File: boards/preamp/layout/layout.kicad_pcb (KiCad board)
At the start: 4 copper layers, 0 parts

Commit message: 2.2 and slave headers moved
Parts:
- added C1: capacitor, C_0603_1608Metric, F.Cu at (32.0, 25.0)
- added C10: capacitor, C_0603_1608Metric, F.Cu at (50.0, 25.0)
- added C11: capacitor, C_0603_1608Metric, F.Cu at (68.0, 25.0)
- added C12: capacitor, C_0603_1608Metric, F.Cu at (86.0, 25.0)
- added C13: capacitor, C_0603_1608Metric, F.Cu at (104.0, 25.0)
- added C14: capacitor, C_0603_1608Metric, F.Cu at (122.0, 25.0)
- added C15: capacitor, C_0603_1608Metric, F.Cu at (140.0, 25.0)
- added C16: capacitor, C_0603_1608Metric, F.Cu at (158.0, 25.0)
- added C17: GRM21BZ71E106KE15K, C_0805_2012Metric, F.Cu at (32.0, 30.0)
- added C18: GRM21BZ71E106KE15K, C_0805_2012Metric, F.Cu at (50.0, 30.0)
- added C19: GRM21BZ71E106KE15K, C_0805_2012Metric, F.Cu at (68.0, 30.0)
- added C2: capacitor, C_0603_1608Metric, F.Cu at (86.0, 30.0)
- added C20: GRM21BZ71E106KE15K, C_0805_2012Metric, F.Cu at (104.0, 30.0)
- added C21: GRM21BZ71E106KE15K, C_0805_2012Metric, F.Cu at (122.0, 30.0)
- added C22: GRM21BZ71E106KE15K, C_0805_2012Metric, F.Cu at (140.0, 30.0)
- added C23: GRM21BZ71E106KE15K, C_0805_2012Metric, F.Cu at (158.0, 30.0)
- added C24: GRM21BZ71E106KE15K, C_0805_2012Metric, F.Cu at (32.0, 35.0)
- added C25: GCM1885C2A103JE02D, C_0603_1608Metric, F.Cu at (50.0, 35.0)
- added C26: GCM1885C2A103JE02D, C_0603_1608Metric, F.Cu at (68.0, 35.0)
- added C27: GCM1885C2A103JE02D, C_0603_1608Metric, F.Cu at (86.0, 35.0)
- added C28: GCM1885C2A103JE02D, C_0603_1608Metric, F.Cu at (104.0, 35.0)
- added C29: GCM1885C2A103JE02D, C_0603_1608Metric, F.Cu at (122.0, 35.0)
- added C3: capacitor, C_0603_1608Metric, F.Cu at (140.0, 35.0)
- added C30: GCM1885C2A103JE02D, C_0603_1608Metric, F.Cu at (158.0, 35.0)
- added C31: GCM1885C2A103JE02D, C_0603_1608Metric, F.Cu at (32.0, 40.0)
- added C32: GCM1885C2A103JE02D, C_0603_1608Metric, F.Cu at (50.0, 40.0)
- added C33: GRM21BZ71E106KE15K, C_0805_2012Metric, F.Cu at (68.0, 40.0)
- added C34: GRM21BZ71E106KE15K, C_0805_2012Metric, F.Cu at (86.0, 40.0)
- added C35: GRM21BZ71E106KE15K, C_0805_2012Metric, F.Cu at (104.0, 40.0)
- added C36: GRM21BZ71E106KE15K, C_0805_2012Metric, F.Cu at (122.0, 40.0)
- added C37: GRM21BZ71E106KE15K, C_0805_2012Metric, F.Cu at (140.0, 40.0)
- added C38: GRM21BZ71E106KE15K, C_0805_2012Metric, F.Cu at (158.0, 40.0)
- added C39: GRM21BZ71E106KE15K, C_0805_2012Metric, F.Cu at (32.0, 45.0)
- added C4: capacitor, C_0603_1608Metric, F.Cu at (50.0, 45.0)
- added C40: GRM21BZ71E106KE15K, C_0805_2012Metric, F.Cu at (68.0, 45.0)
- added C41: capacitor, C_1206_3216Metric, F.Cu at (86.0, 45.0)
- added C42: GRM188R72A104KA35D, C_0603_1608Metric, F.Cu at (104.0, 45.0)
- added C43: GRM21BZ71E106KE15K, C_0805_2012Metric, F.Cu at (122.0, 45.0)
- added C44: GRM188R72A104KA35D, C_0603_1608Metric, F.Cu at (140.0, 45.0)
- added C45: GRM21BZ71E106KE15K, C_0805_2012Metric, F.Cu at (158.0, 45.0)
- added C46: GRM188R72A104KA35D, C_0603_1608Metric, F.Cu at (32.0, 50.0)
- added C47: GRM21BZ71E106KE15K, C_0805_2012Metric, F.Cu at (50.0, 50.0)
- added C48: GRM188R72A104KA35D, C_0603_1608Metric, F.Cu at (68.0, 50.0)
- added C49: GRM21BZ71E106KE15K, C_0805_2012Metric, F.Cu at (86.0, 50.0)
- added C5: capacitor, C_0603_1608Metric, F.Cu at (104.0, 50.0)
- added C50: GRM188R72A104KA35D, C_0603_1608Metric, F.Cu at (122.0, 50.0)
- added C51: GRM21BZ71E106KE15K, C_0805_2012Metric, F.Cu at (140.0, 50.0)
- added C52: GRM188R72A104KA35D, C_0603_1608Metric, F.Cu at (158.0, 50.0)
- added C53: GRM21BZ71E106KE15K, C_0805_2012Metric, F.Cu at (32.0, 55.0)
- added C54: GRM188R72A104KA35D, C_0603_1608Metric, F.Cu at (50.0, 55.0)
- added C55: GRM21BZ71E106KE15K, C_0805_2012Metric, F.Cu at (68.0, 55.0)
- added C56: GRM188R72A104KA35D, C_0603_1608Metric, F.Cu at (86.0, 55.0)
- added C57: GRM21BZ71E106KE15K, C_0805_2012Metric, F.Cu at (104.0, 55.0)
- added C58: GRM188R72A104KA35D, C_0603_1608Metric, F.Cu at (122.0, 55.0)
- added C59: GRM21BZ71E106KE15K, C_0805_2012Metric, F.Cu at (140.0, 55.0)
- added C6: capacitor, C_0603_1608Metric, F.Cu at (158.0, 55.0)
- added C60: GRM188R72A104KA35D, C_0603_1608Metric, F.Cu at (32.0, 60.0)
- added C61: GRM21BZ71E106KE15K, C_0805_2012Metric, F.Cu at (50.0, 60.0)
- added C62: GRM188R72A104KA35D, C_0603_1608Metric, F.Cu at (68.0, 60.0)
- added C63: GRM21BZ71E106KE15K, C_0805_2012Metric, F.Cu at (86.0, 60.0)
- added C64: GRM188R72A104KA35D, C_0603_1608Metric, F.Cu at (104.0, 60.0)
- added C65: GRM21BZ71E106KE15K, C_0805_2012Metric, F.Cu at (122.0, 60.0)
- added C66: GRM188R72A104KA35D, C_0603_1608Metric, F.Cu at (140.0, 60.0)
- added C67: GRM21BZ71E106KE15K, C_0805_2012Metric, F.Cu at (158.0, 60.0)
- added C68: GRM188R72A104KA35D, C_0603_1608Metric, F.Cu at (32.0, 65.0)
- added C69: GRM21BZ71E106KE15K, C_0805_2012Metric, F.Cu at (50.0, 65.0)
- added C7: capacitor, C_0603_1608Metric, F.Cu at (68.0, 65.0)
- added C70: GRM188R72A104KA35D, C_0603_1608Metric, F.Cu at (86.0, 65.0)
- added C71: GRM21BZ71E106KE15K, C_0805_2012Metric, F.Cu at (104.0, 65.0)
- added C72: GRM188R72A104KA35D, C_0603_1608Metric, F.Cu at (122.0, 65.0)
- added C73: GRM21BZ71E106KE15K, C_0805_2012Metric, F.Cu at (140.0, 65.0)
- added C74: GRM188R72A104KA35D, C_0603_1608Metric, F.Cu at (158.0, 65.0)
- added C75: GRM21BZ71E106KE15K, C_0805_2012Metric, F.Cu at (32.0, 70.0)
- added C76: GRM188R72A104KA35D, C_0603_1608Metric, F.Cu at (50.0, 70.0)
- added C8: capacitor, C_0603_1608Metric, F.Cu at (68.0, 70.0)
- added C9: capacitor, C_0603_1608Metric, F.Cu at (86.0, 70.0)
- added H1: ?, MountingHole_3.2mm_M3_DIN965_Pad_TopBottom, F.Cu at (13.0, 13.0)
- added H2: ?, MountingHole_3.2mm_M3_DIN965_Pad_TopBottom, F.Cu at (167.0, 13.0)
- added H3: ?, MountingHole_3.2mm_M3_DIN965_Pad_TopBottom, F.Cu at (13.0, 87.0)
- added H4: ?, MountingHole_3.2mm_M3_DIN965_Pad_TopBottom, F.Cu at (167.0, 87.0)
- added J1: NMJ6HF2, Jack_6.35mm_Neutrik_NMJ6HFD2_Horizontal, F.Cu at (25.0, 75.0)
- added J10: 61300211121, PinHeader_1x02_P2.54mm_Vertical, F.Cu at (133.0, 75.0)
- added J11: 61300211121, PinHeader_1x02_P2.54mm_Vertical, F.Cu at (145.0, 75.0)
- added J12: 61300211121, PinHeader_1x02_P2.54mm_Vertical, F.Cu at (157.0, 75.0)
- added J13: 61300211121, PinHeader_1x02_P2.54mm_Vertical, F.Cu at (25.0, 80.0)
- added J14: 61300211121, PinHeader_1x02_P2.54mm_Vertical, F.Cu at (37.0, 80.0)
- added J15: 61300211121, PinHeader_1x02_P2.54mm_Vertical, F.Cu at (49.0, 80.0)
- added J16: 61300211121, PinHeader_1x02_P2.54mm_Vertical, F.Cu at (61.0, 80.0)
- added J17: 61301021121, PinHeader_2x05_P2.54mm_Vertical, F.Cu at (73.0, 80.0)
- added J18: 61300211121, PinHeader_1x02_P2.54mm_Vertical, F.Cu at (85.0, 80.0)
- added J2: NMJ6HF2, Jack_6.35mm_Neutrik_NMJ6HFD2_Horizontal, F.Cu at (37.0, 75.0)
- added J3: NMJ6HF2, Jack_6.35mm_Neutrik_NMJ6HFD2_Horizontal, F.Cu at (49.0, 75.0)
- added J4: NMJ6HF2, Jack_6.35mm_Neutrik_NMJ6HFD2_Horizontal, F.Cu at (61.0, 75.0)
- added J5: NMJ6HF2, Jack_6.35mm_Neutrik_NMJ6HFD2_Horizontal, F.Cu at (73.0, 75.0)
- added J6: NMJ6HF2, Jack_6.35mm_Neutrik_NMJ6HFD2_Horizontal, F.Cu at (85.0, 75.0)
- added J7: NMJ6HF2, Jack_6.35mm_Neutrik_NMJ6HFD2_Horizontal, F.Cu at (97.0, 75.0)
- added J8: NMJ6HF2, Jack_6.35mm_Neutrik_NMJ6HFD2_Horizontal, F.Cu at (109.0, 75.0)
- added J9: 61300211121, PinHeader_1x02_P2.54mm_Vertical, F.Cu at (121.0, 75.0)
- added R1: ERJ-3EKF7501V, R_0603_1608Metric, F.Cu at (34.0, 25.0)
- added R10: ERJ-3EKF7501V, R_0603_1608Metric, F.Cu at (52.0, 25.0)
- added R11: ERJ-3EKF7501V, R_0603_1608Metric, F.Cu at (70.0, 25.0)
- added R12: ERJ-3EKF7501V, R_0603_1608Metric, F.Cu at (88.0, 25.0)
- added R13: ERJ-3EKF7501V, R_0603_1608Metric, F.Cu at (106.0, 25.0)
- added R14: ERJ-3EKF7501V, R_0603_1608Metric, F.Cu at (124.0, 25.0)
- added R15: ERJ-3EKF7501V, R_0603_1608Metric, F.Cu at (142.0, 25.0)
- added R16: ERJ-3EKF7501V, R_0603_1608Metric, F.Cu at (160.0, 25.0)
- added R17: ERJ-3EKF1004V, R_0603_1608Metric, F.Cu at (34.0, 30.0)
- added R18: ERJ-3EKF1004V, R_0603_1608Metric, F.Cu at (52.0, 30.0)
- added R19: ERJ-3EKF1004V, R_0603_1608Metric, F.Cu at (70.0, 30.0)
- added R2: ERJ-3EKF7501V, R_0603_1608Metric, F.Cu at (88.0, 30.0)
- added R20: ERJ-3EKF1004V, R_0603_1608Metric, F.Cu at (106.0, 30.0)
- added R21: ERJ-3EKF1004V, R_0603_1608Metric, F.Cu at (124.0, 30.0)
- added R22: ERJ-3EKF1004V, R_0603_1608Metric, F.Cu at (142.0, 30.0)
- added R23: ERJ-3EKF1004V, R_0603_1608Metric, F.Cu at (160.0, 30.0)
- added R24: ERJ-3EKF1004V, R_0603_1608Metric, F.Cu at (34.0, 35.0)
- added R25: ERJ-3EKF1002V, R_0603_1608Metric, F.Cu at (52.0, 35.0)
- added R26: ERJ-3EKF1002V, R_0603_1608Metric, F.Cu at (70.0, 35.0)
- added R27: resistor, R_0603_1608Metric, F.Cu at (88.0, 35.0)
- added R28: resistor, R_0603_1608Metric, F.Cu at (106.0, 35.0)
- added R29: resistor, R_0603_1608Metric, F.Cu at (124.0, 35.0)
- added R3: ERJ-3EKF7501V, R_0603_1608Metric, F.Cu at (142.0, 35.0)
- added R30: resistor, R_0603_1608Metric, F.Cu at (160.0, 35.0)
- added R31: resistor, R_0603_1608Metric, F.Cu at (34.0, 40.0)
- added R32: resistor, R_0603_1608Metric, F.Cu at (52.0, 40.0)
- added R33: resistor, R_0603_1608Metric, F.Cu at (70.0, 40.0)
- added R34: resistor, R_0603_1608Metric, F.Cu at (88.0, 40.0)
- added R35: ERJ-3EKF1001V, R_0603_1608Metric, F.Cu at (106.0, 40.0)
- added R36: ERJ-3EKF1001V, R_0603_1608Metric, F.Cu at (124.0, 40.0)
- added R37: ERJ-3EKF1001V, R_0603_1608Metric, F.Cu at (142.0, 40.0)
- added R38: ERJ-3EKF1001V, R_0603_1608Metric, F.Cu at (160.0, 40.0)
- added R39: ERJ-3EKF1001V, R_0603_1608Metric, F.Cu at (34.0, 45.0)
- added R4: ERJ-3EKF7501V, R_0603_1608Metric, F.Cu at (52.0, 45.0)
- added R40: ERJ-3EKF1001V, R_0603_1608Metric, F.Cu at (70.0, 45.0)
- added R41: ERJ-3EKF1001V, R_0603_1608Metric, F.Cu at (88.0, 45.0)
- added R42: ERJ-3EKF1001V, R_0603_1608Metric, F.Cu at (106.0, 45.0)
- added R5: ERJ-3EKF7501V, R_0603_1608Metric, F.Cu at (124.0, 45.0)
- added R6: ERJ-3EKF7501V, R_0603_1608Metric, F.Cu at (142.0, 45.0)
- added R7: ERJ-3EKF7501V, R_0603_1608Metric, F.Cu at (160.0, 45.0)
- added R8: ERJ-3EKF7501V, R_0603_1608Metric, F.Cu at (34.0, 50.0)
- added R9: ERJ-3EKF7501V, R_0603_1608Metric, F.Cu at (52.0, 50.0)
- added RV1: 3296W-1-103LF, Potentiometer_Bourns_3296W_Vertical, F.Cu at (70.0, 50.0)
- added RV2: 3296W-1-103LF, Potentiometer_Bourns_3296W_Vertical, F.Cu at (88.0, 50.0)
- added RV3: 3296W-1-103LF, Potentiometer_Bourns_3296W_Vertical, F.Cu at (106.0, 50.0)
- added RV4: 3296W-1-103LF, Potentiometer_Bourns_3296W_Vertical, F.Cu at (124.0, 50.0)
- added RV5: 3296W-1-103LF, Potentiometer_Bourns_3296W_Vertical, F.Cu at (142.0, 50.0)
- added RV6: 3296W-1-103LF, Potentiometer_Bourns_3296W_Vertical, F.Cu at (160.0, 50.0)
- added RV7: 3296W-1-103LF, Potentiometer_Bourns_3296W_Vertical, F.Cu at (34.0, 55.0)
- added RV8: 3296W-1-103LF, Potentiometer_Bourns_3296W_Vertical, F.Cu at (52.0, 55.0)
- added U1: NE5532DR, SOIC-8_3.9x4.9mm_P1.27mm, F.Cu at (30.0, 30.0)
- added U10: NE5532DR, SOIC-8_3.9x4.9mm_P1.27mm, F.Cu at (48.0, 30.0)
- added U11: NE5532DR, SOIC-8_3.9x4.9mm_P1.27mm, F.Cu at (66.0, 30.0)
- added U12: NE5532DR, SOIC-8_3.9x4.9mm_P1.27mm, F.Cu at (84.0, 30.0)
- added U13: NE5532DR, SOIC-8_3.9x4.9mm_P1.27mm, F.Cu at (102.0, 30.0)
- added U14: NE5532DR, SOIC-8_3.9x4.9mm_P1.27mm, F.Cu at (120.0, 30.0)
- added U15: NE5532DR, SOIC-8_3.9x4.9mm_P1.27mm, F.Cu at (138.0, 30.0)
- added U16: NE5532DR, SOIC-8_3.9x4.9mm_P1.27mm, F.Cu at (156.0, 30.0)
- added U17: NE5532DR, SOIC-8_3.9x4.9mm_P1.27mm, F.Cu at (30.0, 45.0)
- added U2: NE5532DR, SOIC-8_3.9x4.9mm_P1.27mm, F.Cu at (48.0, 45.0)
- added U3: NE5532DR, SOIC-8_3.9x4.9mm_P1.27mm, F.Cu at (66.0, 45.0)
- added U4: NE5532DR, SOIC-8_3.9x4.9mm_P1.27mm, F.Cu at (84.0, 45.0)
- added U5: NE5532DR, SOIC-8_3.9x4.9mm_P1.27mm, F.Cu at (102.0, 45.0)
- added U6: NE5532DR, SOIC-8_3.9x4.9mm_P1.27mm, F.Cu at (120.0, 45.0)
- added U7: NE5532DR, SOIC-8_3.9x4.9mm_P1.27mm, F.Cu at (138.0, 45.0)
- added U8: NE5532DR, SOIC-8_3.9x4.9mm_P1.27mm, F.Cu at (156.0, 45.0)
- added U9: NE5532DR, SOIC-8_3.9x4.9mm_P1.27mm, F.Cu at (30.0, 60.0)
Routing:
- added copper zone on B.Cu, net GND
- added copper zone on F.Cu, net GND
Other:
- board outline added: 160 x 80 mm

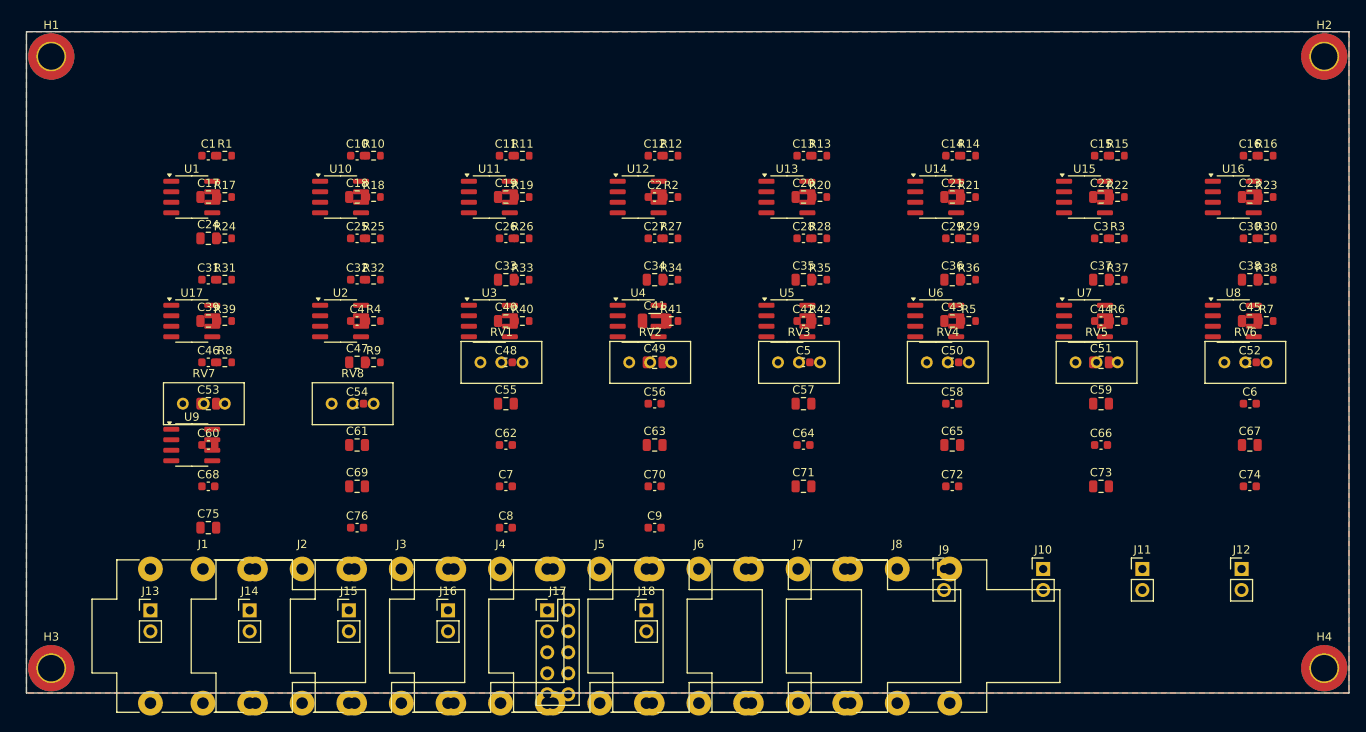
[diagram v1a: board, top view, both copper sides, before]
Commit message: layout changes, main boards smaller
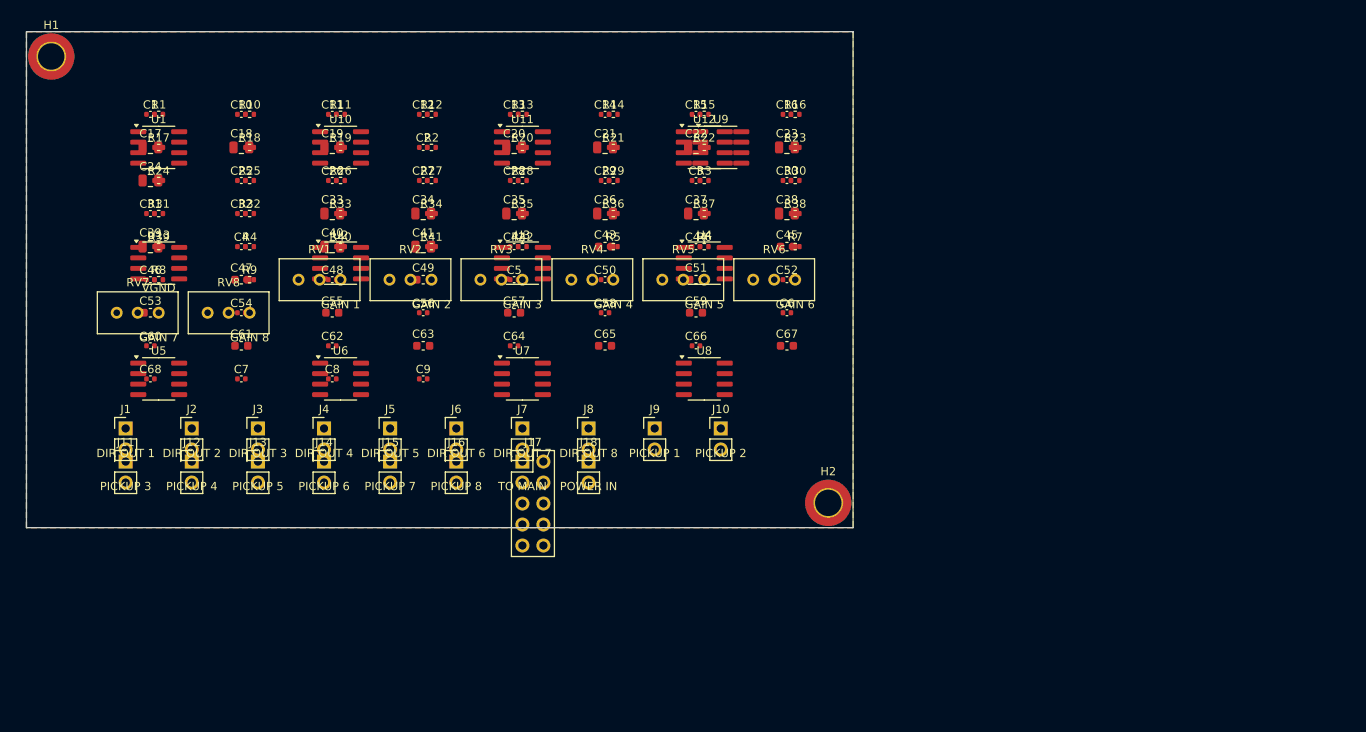
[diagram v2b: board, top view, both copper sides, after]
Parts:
- removed C69, C71, C73, C75: GRM21BZ71E106KE15K, C_0805_2012Metric
- removed C70, C72, C74, C76: GRM188R72A104KA35D, C_0603_1608Metric
- removed H3, H4: ?, MountingHole_3.2mm_M3_DIN965_Pad_TopBottom
- removed U14, U15, U16, U17: NE5532DR, SOIC-8_3.9x4.9mm_P1.27mm
- C1, C10, C11, C12, C13, C14, C15, C16, C2, C3, C4, C5, C6, C7, C8, C9: value capacitor -> GCM1555C1H102FA16D; footprint C_0603_1608Metric -> C_0402_1005Metric
- C25, C26, C27, C28, C29, C30, C31, C32: value GCM1885C2A103JE02D -> GRM1555CYA103GE01D; footprint C_0603_1608Metric -> C_0402_1005Metric
- C41: footprint C_1206_3216Metric -> C_0805_2012Metric
- C42, C44, C46, C48, C50, C52, C54, C56, C58, C60, C62, C64, C66, C68: value GRM188R72A104KA35D -> GCM155R71H104KE02D; footprint C_0603_1608Metric -> C_0402_1005Metric
- C43, C45, C47, C49, C51, C53, C55, C57, C59, C61, C63, C65, C67: value GRM21BZ71E106KE15K -> GRM188Z71A106KA73D; footprint C_0805_2012Metric -> C_0603_1608Metric
- J1, J2, J3, J4, J5, J6, J7, J8: value NMJ6HF2 -> 61300211121; footprint Jack_6.35mm_Neutrik_NMJ6HFD2_Horizontal -> PinHeader_1x02_P2.54mm_Vertical
- R1, R10, R11, R12, R13, R14, R15, R16, R2, R3, R4, R5, R6, R7, R8, R9: value ERJ-3EKF7501V -> ERJ-2RKF7501X; footprint R_0603_1608Metric -> R_0402_1005Metric
- R17, R18, R19, R20, R21, R22, R23, R24: value ERJ-3EKF1004V -> ERJ-2RKF1004X; footprint R_0603_1608Metric -> R_0402_1005Metric
- R25, R26: value ERJ-3EKF1002V -> ERJ-2RKF1002X; footprint R_0603_1608Metric -> R_0402_1005Metric
- R27, R28, R29, R30, R31, R32, R33, R34: footprint R_0603_1608Metric -> R_0402_1005Metric
- R35, R36, R37, R38, R39, R40, R41, R42: value ERJ-3EKF1001V -> ERJ-2RKF1001X; footprint R_0603_1608Metric -> R_0402_1005Metric
- moved J12 127.7 mm to (30.0, 62.0)
- moved J11 123.7 mm to (22.0, 62.0)
- moved H2 80.7 mm to (107.0, 67.0)
- moved U13 76.4 mm to (26.0, 38.0)
- moved U5 76.3 mm to (26.0, 52.0)
- moved U9 73.4 mm to (94.0, 24.0)
- moved U6 72.3 mm to (48.0, 52.0)
- moved U7 68.4 mm to (70.0, 52.0)
- moved U8 64.4 mm to (92.0, 52.0)
- moved RV6 57.9 mm to (103.0, 40.0)
- moved R7 57.7 mm to (103.0, 36.0)
- moved R38 57.6 mm to (103.0, 32.0)
- moved R30 57.4 mm to (103.0, 28.0)
- moved R23 57.3 mm to (103.0, 24.0)
- moved C67 57.3 mm to (102.0, 48.0)
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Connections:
- C17 pad 1: DIRECT_OUT_1 -> BUFFERED_1
- C18 pad 1: DIRECT_OUT_2 -> BUFFERED_2
- C19 pad 1: DIRECT_OUT_3 -> BUFFERED_3
- C20 pad 1: DIRECT_OUT_4 -> BUFFERED_4
- C21 pad 1: DIRECT_OUT_5 -> BUFFERED_5
- C22 pad 1: DIRECT_OUT_6 -> BUFFERED_6
- C23 pad 1: DIRECT_OUT_7 -> BUFFERED_7
- C24 pad 1: DIRECT_OUT_8 -> BUFFERED_8
- U10 pad 1: DIRECT_OUT_3 -> AMPLIFIED_3
- U10 pad 2: DIRECT_OUT_3 -> FB_3
- U10 pad 6: DIRECT_OUT_4 -> FB_4
- U10 pad 7: DIRECT_OUT_4 -> AMPLIFIED_4
- U11 pad 1: DIRECT_OUT_5 -> AMPLIFIED_5
- U11 pad 2: DIRECT_OUT_5 -> FB_5
- U11 pad 6: DIRECT_OUT_6 -> FB_6
- U11 pad 7: DIRECT_OUT_6 -> AMPLIFIED_6
- U12 pad 1: DIRECT_OUT_7 -> AMPLIFIED_7
- U12 pad 2: DIRECT_OUT_7 -> FB_7
- U12 pad 6: DIRECT_OUT_8 -> FB_8
- U12 pad 7: DIRECT_OUT_8 -> AMPLIFIED_8
- U13 pad 1: AMPLIFIED_1 -> VGND
- U13 pad 2: FB_1 -> VGND
- U13 pad 3: BUFFERED_1 -> VGND_MID
- U13 pad 5: BUFFERED_2 -> _IN_P
- U13 pad 6: FB_2 -> _IN_N
- U13 pad 7: AMPLIFIED_2 -> _OUT
- U9 pad 1: DIRECT_OUT_1 -> AMPLIFIED_1
- U9 pad 2: DIRECT_OUT_1 -> FB_1
- U9 pad 6: DIRECT_OUT_2 -> FB_2
- U9 pad 7: DIRECT_OUT_2 -> AMPLIFIED_2
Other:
- board size 160 x 80 mm -> 100 x 60 mm
- board text added: "DIR OUT 1"
- board text added: "DIR OUT 2"
- board text added: "DIR OUT 3"
- board text added: "DIR OUT 4"
- board text added: "DIR OUT 5"
- board text added: "DIR OUT 6"
- board text added: "DIR OUT 7"
- board text added: "DIR OUT 8"
- board text added: "GAIN 1"
- board text added: "GAIN 2"
- board text added: "GAIN 3"
- board text added: "GAIN 4"
- board text added: "GAIN 5"
- board text added: "GAIN 6"
- board text added: "GAIN 7"
- board text added: "GAIN 8"
- board text added: "PICKUP 1"
- board text added: "PICKUP 2"
- board text added: "PICKUP 3"
- board text added: "PICKUP 4"
- board text added: "PICKUP 5"
- board text added: "PICKUP 6"
- board text added: "PICKUP 7"
- board text added: "PICKUP 8"
- board text added: "POWER IN"
- board text added: "TO MAIN"
- board text added: "VGND"

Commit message: layout tweaks
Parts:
- moved R30 86.4 mm to (17.0, 36.0)
- moved J10 85.7 mm to (13.0, 86.0)
- moved RV7 82.2 mm to (104.0, 70.0)
- moved C29 77.1 mm to (27.0, 84.0)
- moved RV8 75.6 mm to (104.0, 79.0)
- moved R39 74.7 mm to (99.0, 52.0)
- moved C39 74.0 mm to (83.0, 82.0)
- moved R1 73.1 mm to (99.0, 16.0)
- moved C27 69.4 mm to (17.0, 84.0)
- moved C67 67.0 mm to (35.0, 46.0)
- moved C26 65.5 mm to (13.0, 84.0)
- moved R29 64.1 mm to (17.0, 32.0)
- moved J8 64.1 mm to (14.0, 54.5)
- moved C31 62.6 mm to (85.0, 14.0)
- moved RV1 60.9 mm to (104.0, 16.0)
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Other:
- board size 100 x 60 mm -> 100 x 80 mm

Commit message: layout fixes
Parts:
- RV1, RV2, RV3, RV4, RV5, RV6, RV7, RV8: value 3296W-1-103LF -> 3314J-1-103E; footprint Potentiometer_Bourns_3296W_Vertical -> Potentiometer_Bourns_3314J_Vertical
- moved C31 86.0 mm to (35.0, 84.0)
- moved C32 74.0 mm to (39.0, 84.0)
- moved C30 72.5 mm to (31.0, 84.0)
- moved C26 71.6 mm to (45.0, 20.0)
- moved R36 60.2 mm to (41.0, 40.0)
- moved C33 56.9 mm to (75.0, 88.0)
- moved C34 47.7 mm to (79.0, 82.0)
- moved C3 46.5 mm to (103.0, 30.0)
- moved R42 39.8 mm to (99.0, 78.0)
- moved R41 39.4 mm to (103.0, 74.0)
- moved R38 38.5 mm to (61.0, 36.0)
- moved C5 38.0 mm to (103.0, 48.0)
- moved C36 36.7 mm to (61.0, 50.0)
- moved C7 20.0 mm to (103.0, 66.0)
- moved C2 14.0 mm to (35.0, 34.0)
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
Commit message: layout
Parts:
- moved C1 77.9 mm to (103.0, 12.0)
- moved C31 77.7 mm to (79.0, 20.0)
- moved C27 69.3 mm to (55.0, 26.0)
- moved C25 64.8 mm to (45.0, 84.0)
- moved R36 59.7 mm to (99.0, 26.0)
- moved R2 58.3 mm to (99.0, 24.0)
- moved C46 57.7 mm to (91.0, 50.0)
- moved C33 56.9 mm to (39.0, 44.0)
- moved C65 56.0 mm to (35.0, 22.0)
- moved R4 50.0 mm to (99.0, 44.0)
- moved C34 47.7 mm to (39.0, 56.0)
- moved R41 46.6 mm to (79.0, 34.0)
- moved C3 46.5 mm to (61.0, 50.0)
- moved C59 45.7 mm to (85.0, 26.0)
- moved R40 42.8 mm to (99.0, 60.0)
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
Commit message: yout
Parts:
- added C69: GCM155R71H104KE02D, C_0402_1005Metric, F.Cu at (57.0, 30.0)
- added C70: GRM188Z71A106KA73D, C_0603_1608Metric, F.Cu at (75.0, 36.0)
- added C71: GCM155R71H104KE02D, C_0402_1005Metric, F.Cu at (79.0, 22.0)
- added C72: GRM188Z71A106KA73D, C_0603_1608Metric, F.Cu at (45.0, 36.0)
- added C73: GCM155R71H104KE02D, C_0402_1005Metric, F.Cu at (45.0, 52.0)
- added U14: NE5532DR, SOIC-8_3.9x4.9mm_P1.27mm, F.Cu at (90.5, 76.4)
- C17, C33: value GRM21BZ71E106KE15K -> GRM1555CYA103GE01D; footprint C_0805_2012Metric -> C_0402_1005Metric
- C25: value GRM1555CYA103GE01D -> GRM21BZ71E106KE15K; footprint C_0402_1005Metric -> C_0805_2012Metric
- C41: value capacitor -> GRM21BZ71E106KE15K
- C42: value GCM155R71H104KE02D -> GRM21BZ71E106KE15K; footprint C_0402_1005Metric -> C_0805_2012Metric
- C43, C45, C47, C49, C51, C53, C55, C57, C59, C61, C63, C65, C67: value GRM188Z71A106KA73D -> GCM155R71H104KE02D; footprint C_0603_1608Metric -> C_0402_1005Metric
- C44: value GCM155R71H104KE02D -> capacitor; footprint C_0402_1005Metric -> C_0805_2012Metric
- C46, C48, C50, C52, C54, C56, C58, C60, C62, C64, C66, C68: value GCM155R71H104KE02D -> GRM188Z71A106KA73D; footprint C_0402_1005Metric -> C_0603_1608Metric
- U5: value NE5532DR -> LP2985-33DBVR; footprint SOIC-8_3.9x4.9mm_P1.27mm -> SOT-23-5
- moved C28 75.5 mm to (21.0, 84.0)
- moved C27 70.5 mm to (15.0, 84.0)
- moved C26 66.0 mm to (51.0, 84.0)
- moved C41 58.2 mm to (85.0, 56.0)
- moved R35 56.9 mm to (51.0, 30.0)
- moved C35 56.9 mm to (39.0, 44.0)
- moved C46 56.0 mm to (35.0, 48.0)
- moved C68 56.0 mm to (35.0, 22.0)
- moved C25 54.3 mm to (39.0, 30.0)
- moved C1 51.3 mm to (55.0, 30.0)
- moved C59 50.6 mm to (35.0, 18.0)
- moved C32 50.2 mm to (35.0, 34.0)
- moved R36 50.0 mm to (51.0, 40.0)
- moved C34 48.2 mm to (75.0, 88.0)
- moved J18 48.1 mm to (95.0, 87.0), turned to 90 degrees
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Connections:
- C17 pad 1: BUFFERED_1 -> AVDD_BYP
- C17 pad 2: DIRECT_AC_1 -> GND
- C18 pad 1: BUFFERED_2 -> BUFFERED_1
- C18 pad 2: DIRECT_AC_2 -> DIRECT_AC_1
- C19 pad 1: BUFFERED_3 -> BUFFERED_2
- C19 pad 2: DIRECT_AC_3 -> DIRECT_AC_2
- C20 pad 1: BUFFERED_4 -> BUFFERED_3
- C20 pad 2: DIRECT_AC_4 -> DIRECT_AC_3
- C21 pad 1: BUFFERED_5 -> BUFFERED_4
- C21 pad 2: DIRECT_AC_5 -> DIRECT_AC_4
- C22 pad 1: BUFFERED_6 -> BUFFERED_5
- C22 pad 2: DIRECT_AC_6 -> DIRECT_AC_5
- C23 pad 1: BUFFERED_7 -> BUFFERED_6
- C23 pad 2: DIRECT_AC_7 -> DIRECT_AC_6
- C24 pad 1: BUFFERED_8 -> BUFFERED_7
- C24 pad 2: DIRECT_AC_8 -> DIRECT_AC_7
- C25 pad 1: PICKUP_1 -> BUFFERED_8
- C25 pad 2: COUPLED_1 -> DIRECT_AC_8
- C26 pad 1: PICKUP_2 -> PICKUP_1
- C26 pad 2: COUPLED_2 -> COUPLED_1
- C27 pad 1: PICKUP_3 -> PICKUP_2
- C27 pad 2: COUPLED_3 -> COUPLED_2
- C28 pad 1: PICKUP_4 -> PICKUP_3
- C28 pad 2: COUPLED_4 -> COUPLED_3
- C29 pad 1: PICKUP_5 -> PICKUP_4
- C29 pad 2: COUPLED_5 -> COUPLED_4
- C30 pad 1: PICKUP_6 -> PICKUP_5
- C30 pad 2: COUPLED_6 -> COUPLED_5
- C31 pad 1: PICKUP_7 -> PICKUP_6
- C31 pad 2: COUPLED_7 -> COUPLED_6
- C32 pad 1: PICKUP_8 -> PICKUP_7
- C32 pad 2: COUPLED_8 -> COUPLED_7
- C33 pad 1: FILTERED_1 -> PICKUP_8
- C33 pad 2: SIGNAL_1 -> COUPLED_8
- C34 pad 1: FILTERED_2 -> FILTERED_1
- C34 pad 2: SIGNAL_2 -> SIGNAL_1
- C35 pad 1: FILTERED_3 -> FILTERED_2
- C35 pad 2: SIGNAL_3 -> SIGNAL_2
- C36 pad 1: FILTERED_4 -> FILTERED_3
- C36 pad 2: SIGNAL_4 -> SIGNAL_3
- C37 pad 1: FILTERED_5 -> FILTERED_4
- C37 pad 2: SIGNAL_5 -> SIGNAL_4
- C38 pad 1: FILTERED_6 -> FILTERED_5
- C38 pad 2: SIGNAL_6 -> SIGNAL_5
- C39 pad 1: FILTERED_7 -> FILTERED_6
- C39 pad 2: SIGNAL_7 -> SIGNAL_6
- C40 pad 1: FILTERED_8 -> FILTERED_7
- C40 pad 2: SIGNAL_8 -> SIGNAL_7
- C41 pad 1: VGND -> FILTERED_8
- C41 pad 2: GND -> SIGNAL_8
- C42 pad 1: VGND -> VBAT
- C43 pad 1: AVDD -> VBAT
- C44 pad 1: AVDD -> VGND
- C45 pad 1: AVDD -> VGND
- J17 pad 9: AVDD -> VBAT
- J18 pad 1: AVDD -> VBAT
- U10 pad 1: AMPLIFIED_3 -> AMPLIFIED_1
- U10 pad 2: FB_3 -> FB_1
- U10 pad 3: BUFFERED_3 -> BUFFERED_1
- U10 pad 5: BUFFERED_4 -> BUFFERED_2
- U10 pad 6: FB_4 -> FB_2
- U10 pad 7: AMPLIFIED_4 -> AMPLIFIED_2
- U11 pad 1: AMPLIFIED_5 -> AMPLIFIED_3
- U11 pad 2: FB_5 -> FB_3
- U11 pad 3: BUFFERED_5 -> BUFFERED_3
- U11 pad 5: BUFFERED_6 -> BUFFERED_4
- U11 pad 6: FB_6 -> FB_4
- U11 pad 7: AMPLIFIED_6 -> AMPLIFIED_4
- U12 pad 1: AMPLIFIED_7 -> AMPLIFIED_5
- U12 pad 2: FB_7 -> FB_5
- U12 pad 3: BUFFERED_7 -> BUFFERED_5
- U12 pad 5: BUFFERED_8 -> BUFFERED_6
- U12 pad 6: FB_8 -> FB_6
- U12 pad 7: AMPLIFIED_8 -> AMPLIFIED_6
- U13 pad 1: VGND -> AMPLIFIED_7
- U13 pad 2: VGND -> FB_7
- U13 pad 3: VGND_MID -> BUFFERED_7
- U13 pad 5: _IN_P -> BUFFERED_8
- U13 pad 6: _IN_N -> FB_8
- U13 pad 7: _OUT -> AMPLIFIED_8
- U5 pad 1: BUFFERED_1 -> VBAT
- U5 pad 2: BUFFERED_1 -> GND
- U5 pad 3: COUPLED_1 -> VBAT
- U5 pad 4: GND -> AVDD_BYP
- U5 pad 5: COUPLED_2 -> AVDD
- U6 pad 1: BUFFERED_3 -> BUFFERED_1
- U6 pad 2: BUFFERED_3 -> BUFFERED_1
- U6 pad 3: COUPLED_3 -> COUPLED_1
- U6 pad 5: COUPLED_4 -> COUPLED_2
- U6 pad 6: BUFFERED_4 -> BUFFERED_2
- U6 pad 7: BUFFERED_4 -> BUFFERED_2
- U7 pad 1: BUFFERED_5 -> BUFFERED_3
- U7 pad 2: BUFFERED_5 -> BUFFERED_3
- U7 pad 3: COUPLED_5 -> COUPLED_3
- U7 pad 5: COUPLED_6 -> COUPLED_4
- U7 pad 6: BUFFERED_6 -> BUFFERED_4
- U7 pad 7: BUFFERED_6 -> BUFFERED_4
- U8 pad 1: BUFFERED_7 -> BUFFERED_5
- U8 pad 2: BUFFERED_7 -> BUFFERED_5
- U8 pad 3: COUPLED_7 -> COUPLED_5
- U8 pad 5: COUPLED_8 -> COUPLED_6
- U8 pad 6: BUFFERED_8 -> BUFFERED_6
- U8 pad 7: BUFFERED_8 -> BUFFERED_6
- U9 pad 1: AMPLIFIED_1 -> BUFFERED_7
- U9 pad 2: FB_1 -> BUFFERED_7
- U9 pad 3: BUFFERED_1 -> COUPLED_7
- U9 pad 5: BUFFERED_2 -> COUPLED_8
- U9 pad 6: FB_2 -> BUFFERED_8
- U9 pad 7: AMPLIFIED_2 -> BUFFERED_8
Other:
- board text added: "AVDD LDO"

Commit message: ground plane moat etc
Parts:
- moved C30 88.4 mm to (85.0, 14.0)
- moved C28 77.7 mm to (65.0, 20.0)
- moved C31 76.6 mm to (35.0, 84.0)
- moved C34 56.9 mm to (39.0, 44.0)
- moved C35 56.9 mm to (75.0, 88.0)
- moved R41 55.3 mm to (49.0, 62.0)
- moved R36 50.6 mm to (99.0, 24.0)
- moved R7 50.0 mm to (55.0, 68.0)
- moved R42 49.2 mm to (55.0, 56.0)
- moved C36 45.3 mm to (49.0, 48.0)
- moved R8 42.0 mm to (61.0, 62.0)
- moved C37 41.2 mm to (49.0, 52.0)
- moved C40 34.9 mm to (85.0, 56.0)
- moved C24 33.5 mm to (39.0, 30.0)
- moved R5 32.8 mm to (103.0, 56.0)
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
